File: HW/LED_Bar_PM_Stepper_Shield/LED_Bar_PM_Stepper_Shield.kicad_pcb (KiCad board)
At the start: 2 copper layers, 50.8 x 30.5 mm, 3 parts, among them J1 1x14 2.54mm female, J2 1x14 2.54mm female

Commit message: Done something.
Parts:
- removed J2: 1x14 2.54mm female, Connector_PinSocket_2.54mm:PinSocket_1x14_P2.54mm_Vertical
- added C1: 100n, Capacitor_SMD:C_0603_1608Metric, F.Cu at (161.8, 78.8)
- added C2: 100n, Capacitor_SMD:C_0603_1608Metric, F.Cu at (161.8, 81.3)
- added J3: JST XH 5pin male socket, Connector_JST:JST_XH_B5B-XH-A_1x05_P2.50mm_Vertical, F.Cu at (146.3, 88.7)
- added RN1: 8x470, Resistor_THT:R_Array_SIP9, F.Cu at (145.1, 75.3)
- J1: value 1x14 2.54mm female -> JST XH 5pin male socket; footprint Connector_PinSocket_2.54mm:PinSocket_1x14_P2.54mm_Vertical -> Connector_JST:JST_XH_B5B-XH-A_1x05_P2.50mm_Vertical
- moved J1 49.9 mm to (146.3, 80.9), turned to 0 degrees
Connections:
- J1 pad 1: /D3__D6 -> +5V
- J1 pad 2: /D4__D7 -> /Untitled Sheet/O5
- J1 pad 3: /D5__D8 -> /Untitled Sheet/O6
- J1 pad 4: /D6__D9 -> /Untitled Sheet/O7
- J1 pad 5: /D7__D10 -> /Untitled Sheet/O8
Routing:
- net +5V: track 68.6 -> 0.00 mm, vias 4 -> 0
- net GND: track 38.1 -> 0.00 mm, vias 2 -> 0
- net /D10__AIN0: track 30.5 -> 0.00 mm, vias 2 -> 0
- net /A0__AIN2: track 22.9 -> 0.00 mm, vias 2 -> 0
- net /D2__D5: track 15.2 -> 0.00 mm
- net /D12__AIN3: track 12.7 -> 0.00 mm
- net /D11__AIN4: track 12.7 -> 0.00 mm
- net /A5__D4: track 2.54 -> 0.00 mm
- net /A4__D3: track 2.54 -> 0.00 mm
- net /A3__D2: track 2.54 -> 0.00 mm
- net /A2__D1: track 2.54 -> 0.00 mm
- net /A1__D0: track 2.54 -> 0.00 mm
- net /D9__D12: track 2.54 -> 0.00 mm
- net /D8__D11: track 2.54 -> 0.00 mm
- net /D7__D10: track 2.54 -> 0.00 mm
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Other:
- board size 50.8 x 30.5 mm -> 50.8 x 25.4 mm

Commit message: Done PCB.
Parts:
- removed C1, C2: 100n, Capacitor_SMD:C_0603_1608Metric
- added D1: LED_Bar_10, Package_DIP:DIP-20_W7.62mm_Socket, F.Cu at (170.2, 109.2)
- added D2: LED_Bar_10, Package_DIP:DIP-20_W7.62mm_Socket, F.Cu at (221.0, 88.9)
- added H1: M3, MountingHole:MountingHole_3.2mm_M3, F.Cu at (86.4, 129.5)
- added H2: M3, MountingHole:MountingHole_3.2mm_M3, F.Cu at (86.4, 83.8)
- added H3: M3, MountingHole:MountingHole_3.2mm_M3, F.Cu at (233.7, 129.5)
- added H4: M3, MountingHole:MountingHole_3.2mm_M3, F.Cu at (231.1, 83.8)
- added J3: JST XH 5pin male socket, Connector_JST:JST_XH_B5B-XH-A_1x05_P2.50mm_Vertical, F.Cu at (203.2, 109.1)
- added J4: JST XH 5pin male socket, Connector_JST:JST_XH_B5B-XH-A_1x05_P2.50mm_Vertical, F.Cu at (213.4, 86.4)
- added J5: 1x6 2.54mm female, pin2 filled, Connector_PinHeader_2.54mm:PinHeader_1x06_P2.54mm_Vertical, F.Cu at (99.1, 83.8)
- added J6: 1x6 2.54mm female, pin2 filled, Connector_PinHeader_2.54mm:PinHeader_1x06_P2.54mm_Vertical, F.Cu at (83.8, 121.9)
- added RN2: 8x470, Resistor_THT:R_Array_SIP9, F.Cu at (233.7, 109.2)
- added U1: ULN2803A, Package_DIP:DIP-20_W7.62mm_Socket, F.Cu at (137.2, 104.1)
- added U2: ULN2803A, Package_DIP:DIP-20_W7.62mm_Socket, F.Cu at (188.0, 83.8)
- moved RN1 66.1 mm to (182.9, 129.5), turned to 90 degrees
- moved A1 62.9 mm to (127.0, 127.0), turned to 180 degrees
- moved J1 41.2 mm to (152.4, 129.4), turned to 90 degrees
- moved J2 30.6 mm to (162.6, 106.8), turned to -90 degrees
- renumbered J3 to J1, J1 to J2
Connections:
- A1 pad 1: unconnected-(A1-D1/TX-Pad1) -> /b0/B1
- A1 pad 10: /D7__D10 -> /b0/B7
- A1 pad 11: /D8__D11 -> /b1/B0
- A1 pad 12: /D9__D12 -> /b1/B1
- A1 pad 13: /D10__AIN0 -> /b1/B2
- A1 pad 14: /D11__AIN4 -> /b1/B3
- A1 pad 15: /D12__AIN3 -> /DB0
- A1 pad 16: unconnected-(A1-D13-Pad16) -> /DA0
- A1 pad 19: /A0__AIN2 -> /L0
- A1 pad 2: unconnected-(A1-D0/RX-Pad2) -> /b0/B0
- A1 pad 20: /A1__D0 -> /L1
- A1 pad 21: /A2__D1 -> /L2
- A1 pad 22: /A3__D2 -> /L3
- A1 pad 23: /A4__D3 -> /DB1
- A1 pad 24: /A5__D4 -> /DA1
- A1 pad 25: unconnected-(A1-A6-Pad25) -> /A0
- A1 pad 26: unconnected-(A1-A7-Pad26) -> /A1
- A1 pad 29: unconnected-(A1-GND-Pad29) -> GND
- A1 pad 5: /D2__D5 -> /b0/B2
- A1 pad 6: /D3__D6 -> /b0/B3
- A1 pad 7: /D4__D7 -> /b0/B4
- A1 pad 8: /D5__D8 -> /b0/B5
- A1 pad 9: /D6__D9 -> /b0/B6
- J1 pad 2: /Untitled Sheet/O1 -> /b0/O0
- J1 pad 3: /Untitled Sheet/O2 -> /b0/O1
- J1 pad 4: /Untitled Sheet/O3 -> /b0/O2
- J1 pad 5: /Untitled Sheet/O4 -> /b0/O3
- J2 pad 2: /Untitled Sheet/O5 -> /b0/O7
- J2 pad 3: /Untitled Sheet/O6 -> /b0/O6
- J2 pad 4: /Untitled Sheet/O7 -> /b0/O5
- J2 pad 5: /Untitled Sheet/O8 -> /b0/O4
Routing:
- net +5V: track 0.00 -> 297.4 mm, vias 0 -> 11
- net GND: track 0.00 -> 198.1 mm, vias 0 -> 8
- net /L0: track 0.00 -> 127.0 mm, vias 0 -> 4
- net /L3: track 0.00 -> 104.1 mm, vias 0 -> 2
- net /L2: track 0.00 -> 104.1 mm, vias 0 -> 2
- net /L1: track 0.00 -> 104.1 mm, vias 0 -> 2
- net /b1/B3: track 0.00 -> 61.0 mm
- net /b1/B2: track 0.00 -> 61.0 mm
- net /b1/B1: track 0.00 -> 61.0 mm
- net /b1/B0: track 0.00 -> 61.0 mm
- net /A0: track 0.00 -> 53.3 mm, vias 0 -> 2
- net /DA1: track 0.00 -> 40.6 mm, vias 0 -> 4
- net /DB1: track 0.00 -> 27.9 mm
- net /A1: track 0.00 -> 27.9 mm
- net /DB0: track 0.00 -> 27.9 mm, vias 0 -> 2
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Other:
- board size 50.8 x 25.4 mm -> 157.5 x 55.9 mm

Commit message: Small corrections.
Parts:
- added J7: Extension of Ard Nano, Connector_PinSocket_2.54mm:PinSocket_1x01_P2.54mm_Vertical, F.Cu at (111.8, 129.5)
- added J8: Extension of Ard Nano, Connector_PinSocket_2.54mm:PinSocket_1x01_P2.54mm_Vertical, F.Cu at (127.0, 129.5)
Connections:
- A1 pad 4: GND -> unconnected-(A1-GND-Pad4)
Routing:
- net GND: track 198.1 -> 200.7 mm
- net +5V: vias 11 -> 10

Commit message: Correcting PCB
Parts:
- J7, J8: value Extension of Ard Nano -> Extension of Ard Nano, filled
- U1, U2: footprint Package_DIP:DIP-20_W7.62mm_Socket -> Package_DIP:DIP-18_W7.62mm_Socket
- moved J1 5.12 mm to (152.4, 124.3)
- moved D1 5.08 mm to (170.2, 104.1)
- moved J2 5.08 mm to (162.6, 101.8)
- moved RN1 5.08 mm to (182.9, 124.5)
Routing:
- net +5V: track 297.4 -> 183.2 mm, vias 10 -> 9
- net /b0/O0: track 25.5 -> 0.00 mm
- net /b0/O7: track 25.4 -> 0.00 mm
- net /b0/O6: track 25.4 -> 0.00 mm
- net /b0/O5: track 25.4 -> 0.00 mm
- net /b0/O3: track 25.4 -> 0.00 mm
- net /b0/O2: track 25.4 -> 0.00 mm
- net /b0/O1: track 25.4 -> 0.00 mm
- net /b1/B0: track 61.0 -> 43.2 mm
- net Net-(RN1-R8): track 5.08 -> 0.00 mm
- net Net-(RN1-R7): track 5.08 -> 0.00 mm
- net Net-(RN1-R6): track 5.08 -> 0.00 mm
- net Net-(RN1-R5): track 5.08 -> 0.00 mm
- net Net-(RN1-R4): track 5.08 -> 0.00 mm
- net Net-(RN1-R3): track 5.08 -> 0.00 mm
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
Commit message: PCB corrected.
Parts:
- moved H4 10.2 mm to (241.3, 83.8)
- moved H3 7.62 mm to (241.3, 129.5)
- moved D2 5.08 mm to (221.0, 83.8)
- moved J3 5.08 mm to (203.2, 104.0)
- moved RN2 5.08 mm to (233.7, 104.1)
- moved J4 4.96 mm to (213.4, 81.4)
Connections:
- D1 pad 10: GND -> unconnected-(D1-Pad10)
- D1 pad 11: GND -> unconnected-(D1-Pad11)
- D2 pad 10: GND -> unconnected-(D2-Pad10)
- D2 pad 11: GND -> unconnected-(D2-Pad11)
- J7 pad 1: +5V -> GND
- J8 pad 1: +5V -> GND
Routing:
- net +5V: track 183.2 -> 297.5 mm, vias 9 -> 14
- net /b1/B0: track 43.2 -> 71.1 mm, vias 0 -> 2
- net /b0/O7: track 0.00 -> 25.4 mm
- net /b0/O6: track 0.00 -> 25.4 mm
- net /b0/O5: track 0.00 -> 25.4 mm
- net /b0/O3: track 0.00 -> 25.4 mm
- net /b0/O2: track 0.00 -> 25.4 mm
- net /b0/O1: track 0.00 -> 25.4 mm
- net /b0/O0: track 0.00 -> 25.4 mm
- net GND: track 200.7 -> 193.0 mm
- net Net-(RN2-R8): track 0.00 -> 5.08 mm
- net Net-(RN2-R7): track 0.00 -> 5.08 mm
- net Net-(RN2-R6): track 0.00 -> 5.08 mm
- net Net-(RN2-R5): track 0.00 -> 5.08 mm
- net Net-(RN2-R4): track 0.00 -> 5.08 mm
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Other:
- board size 157.5 x 55.9 mm -> 165.1 x 55.9 mm

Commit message: Resistors.
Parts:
- added R1: 10k, For_Rasterboard:R_Axial_DIN0207_L6.3mm_D2.5mm_Pinf_Horizontal, F.Cu at (109.2, 121.9)
- added R2: 10k, For_Rasterboard:R_Axial_DIN0207_L6.3mm_D2.5mm_Pinf_Horizontal, F.Cu at (119.4, 119.4)
- added R3: 10k, For_Rasterboard:R_Axial_DIN0207_L6.3mm_D2.5mm_Pinf_Horizontal, F.Cu at (114.3, 109.2)
- added R4: 10k, For_Rasterboard:R_Axial_DIN0207_L6.3mm_D2.5mm_Pinf_Horizontal, F.Cu at (116.8, 109.2)
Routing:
- net GND: track 193.0 -> 243.8 mm, vias 8 -> 12
- net /DA0: track 12.7 -> 25.4 mm, vias 0 -> 1
- net /DB1: track 27.9 -> 38.1 mm, vias 0 -> 1
- net /DB0: track 27.9 -> 33.0 mm, vias 2 -> 3
- net /L0: track 127.0 -> 124.5 mm
- net /DA1: track 40.6 -> 43.2 mm, vias 4 -> 5

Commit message: Correction.
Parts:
- added JP1: Jumper_2_Open, Connector_PinHeader_2.54mm:PinHeader_1x02_P2.54mm_Vertical, F.Cu at (104.1, 119.4)
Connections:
- A1 pad 27: +5V -> Net-(A1-+5V)
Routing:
- net Net-(A1-+5V): track 0.00 -> 7.62 mm
- net GND: track 243.8 -> 246.4 mm
- net +5V: track 297.5 -> 295.0 mm

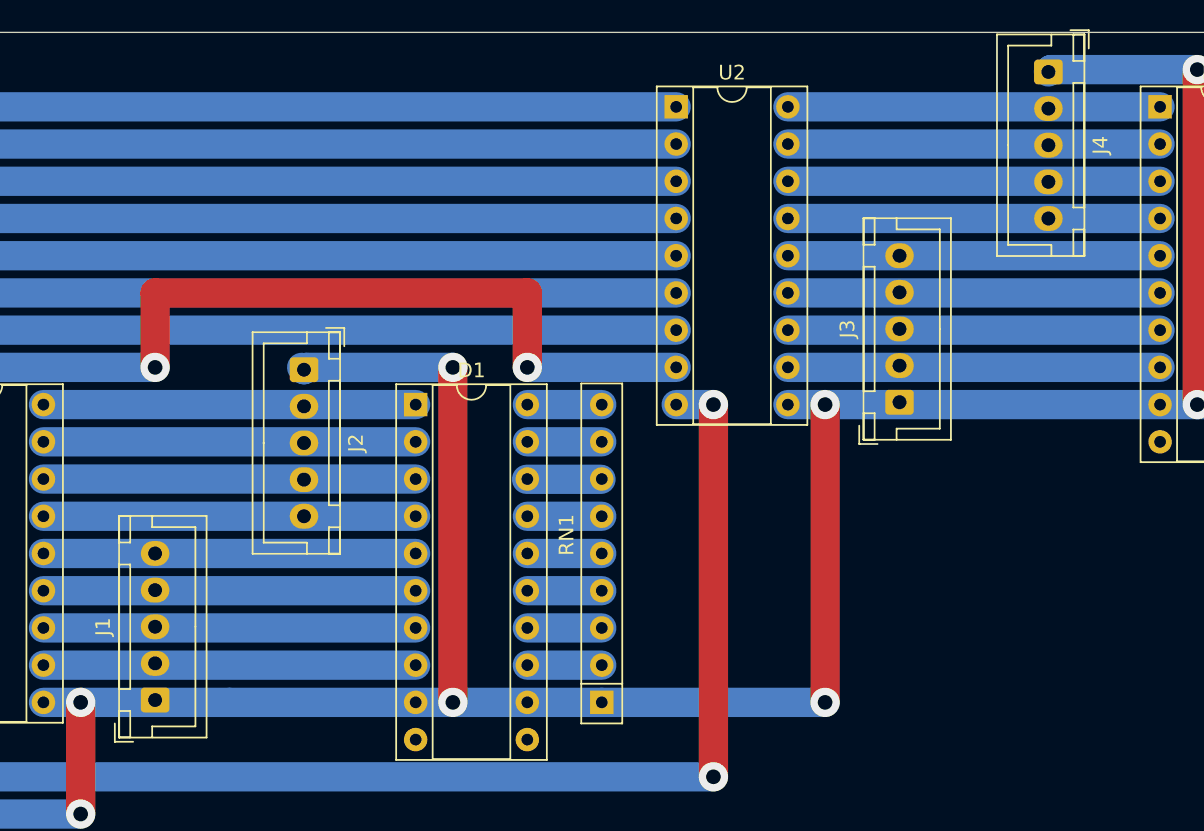
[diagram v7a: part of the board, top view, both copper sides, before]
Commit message: Connector orientations correction.
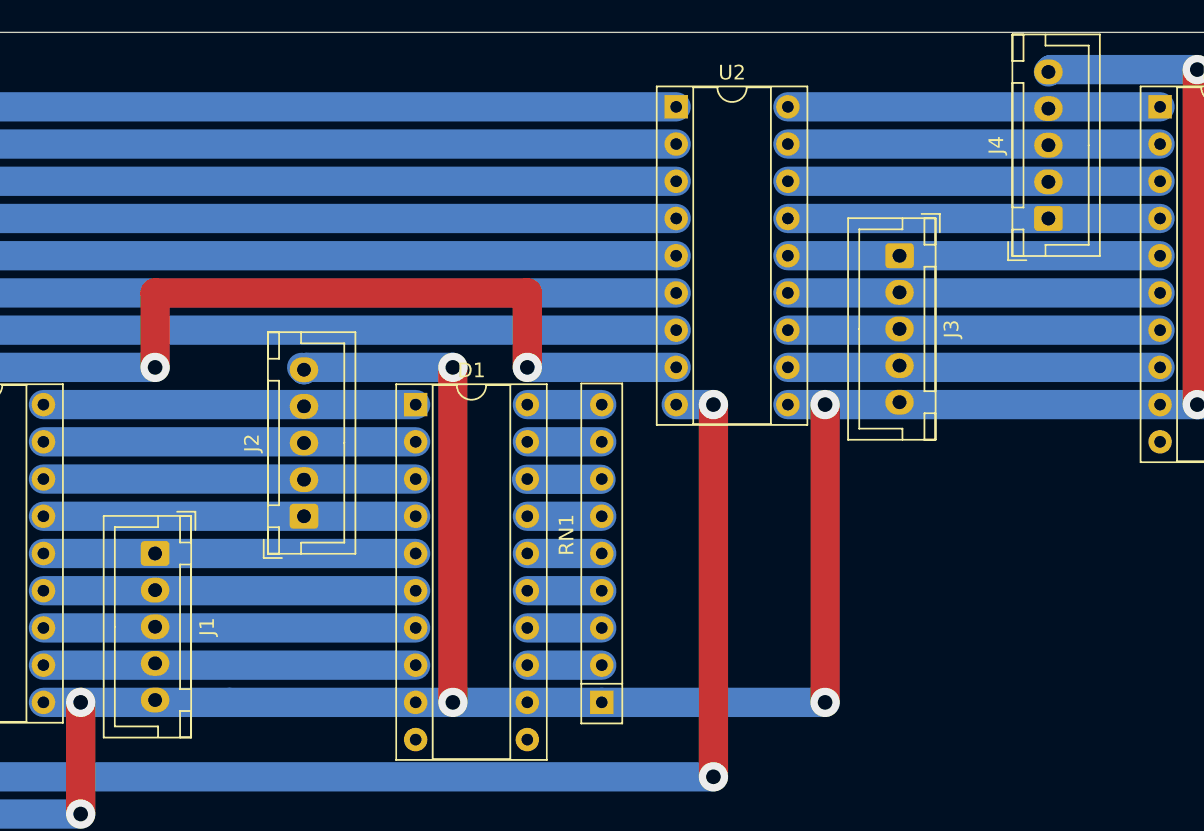
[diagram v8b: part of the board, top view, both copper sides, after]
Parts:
- moved J1 10.0 mm to (152.4, 114.3), turned to -90 degrees
- moved J2 10.0 mm to (162.6, 111.8), turned to 90 degrees
- moved J3 10.0 mm to (203.2, 94.0), turned to -90 degrees
- moved J4 10.0 mm to (213.4, 91.4), turned to 90 degrees
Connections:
- J1 pad 1: +5V -> /b0/O3
- J1 pad 2: /b0/O0 -> /b0/O2
- J1 pad 4: /b0/O2 -> /b0/O0
- J1 pad 5: /b0/O3 -> +5V
- J2 pad 1: +5V -> /b0/O4
- J2 pad 2: /b0/O7 -> /b0/O5
- J2 pad 4: /b0/O5 -> /b0/O7
- J2 pad 5: /b0/O4 -> +5V
- J3 pad 1: +5V -> /b1/O3
- J3 pad 2: /b1/O0 -> /b1/O2
- J3 pad 4: /b1/O2 -> /b1/O0
- J3 pad 5: /b1/O3 -> +5V
- J4 pad 1: +5V -> /b1/O4
- J4 pad 2: /b1/O7 -> /b1/O5
- J4 pad 4: /b1/O5 -> /b1/O7
- J4 pad 5: /b1/O4 -> +5V
